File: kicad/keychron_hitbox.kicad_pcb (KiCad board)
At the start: 2 copper layers, 208.5 x 125 mm, 55 parts, among them U1 RP2040-Zero

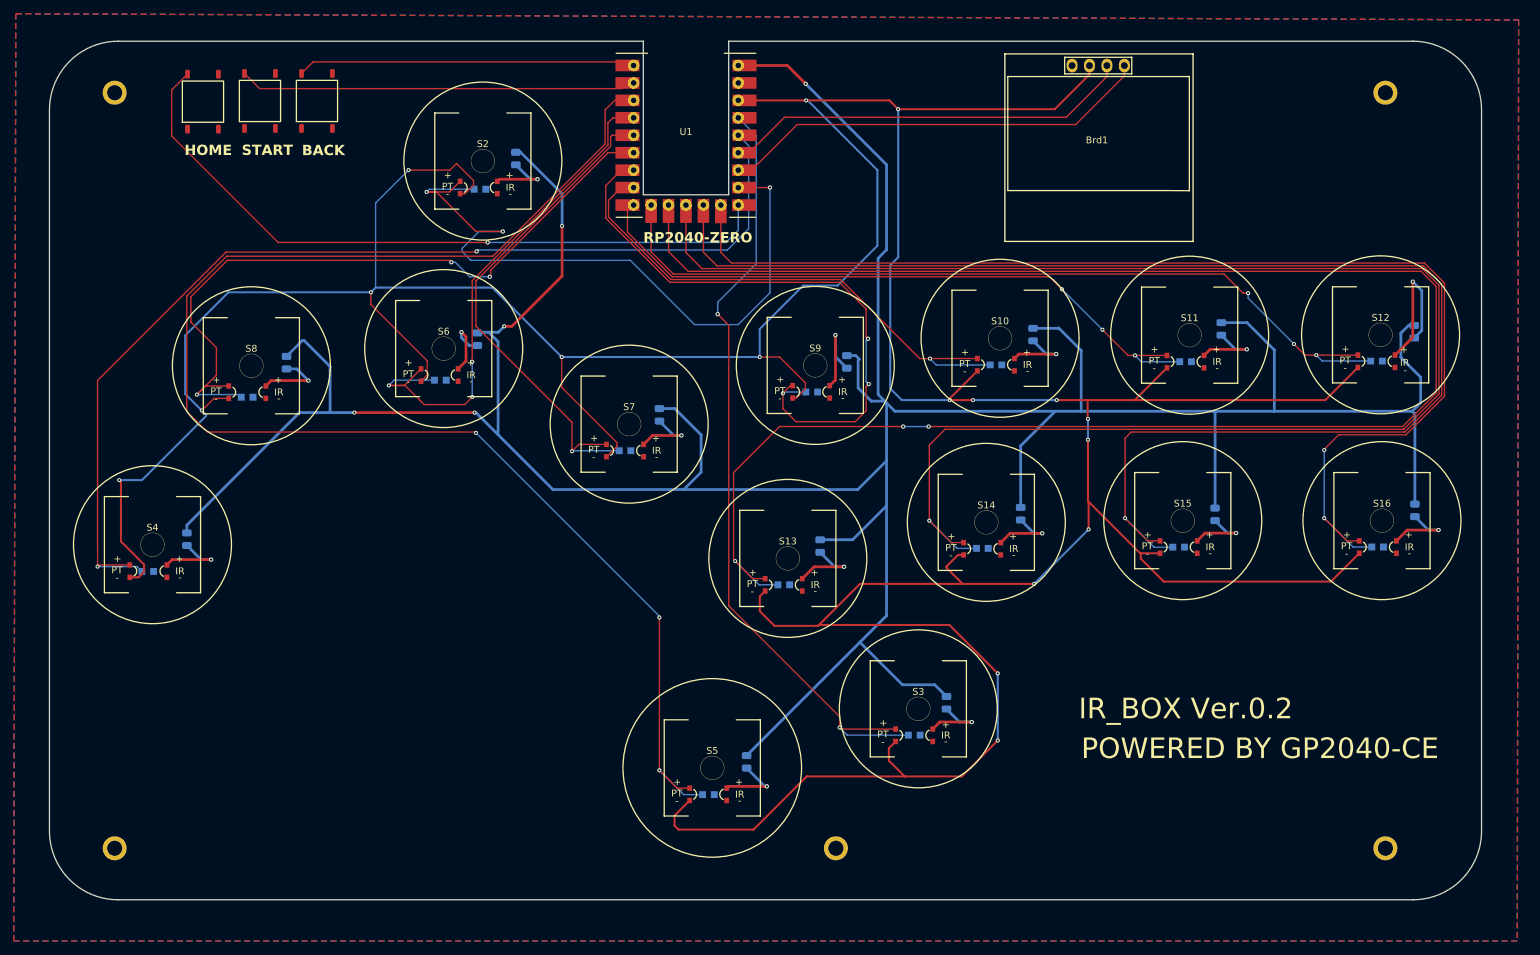
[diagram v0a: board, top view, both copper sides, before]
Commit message: updated seating for OLED & some acrylic designs
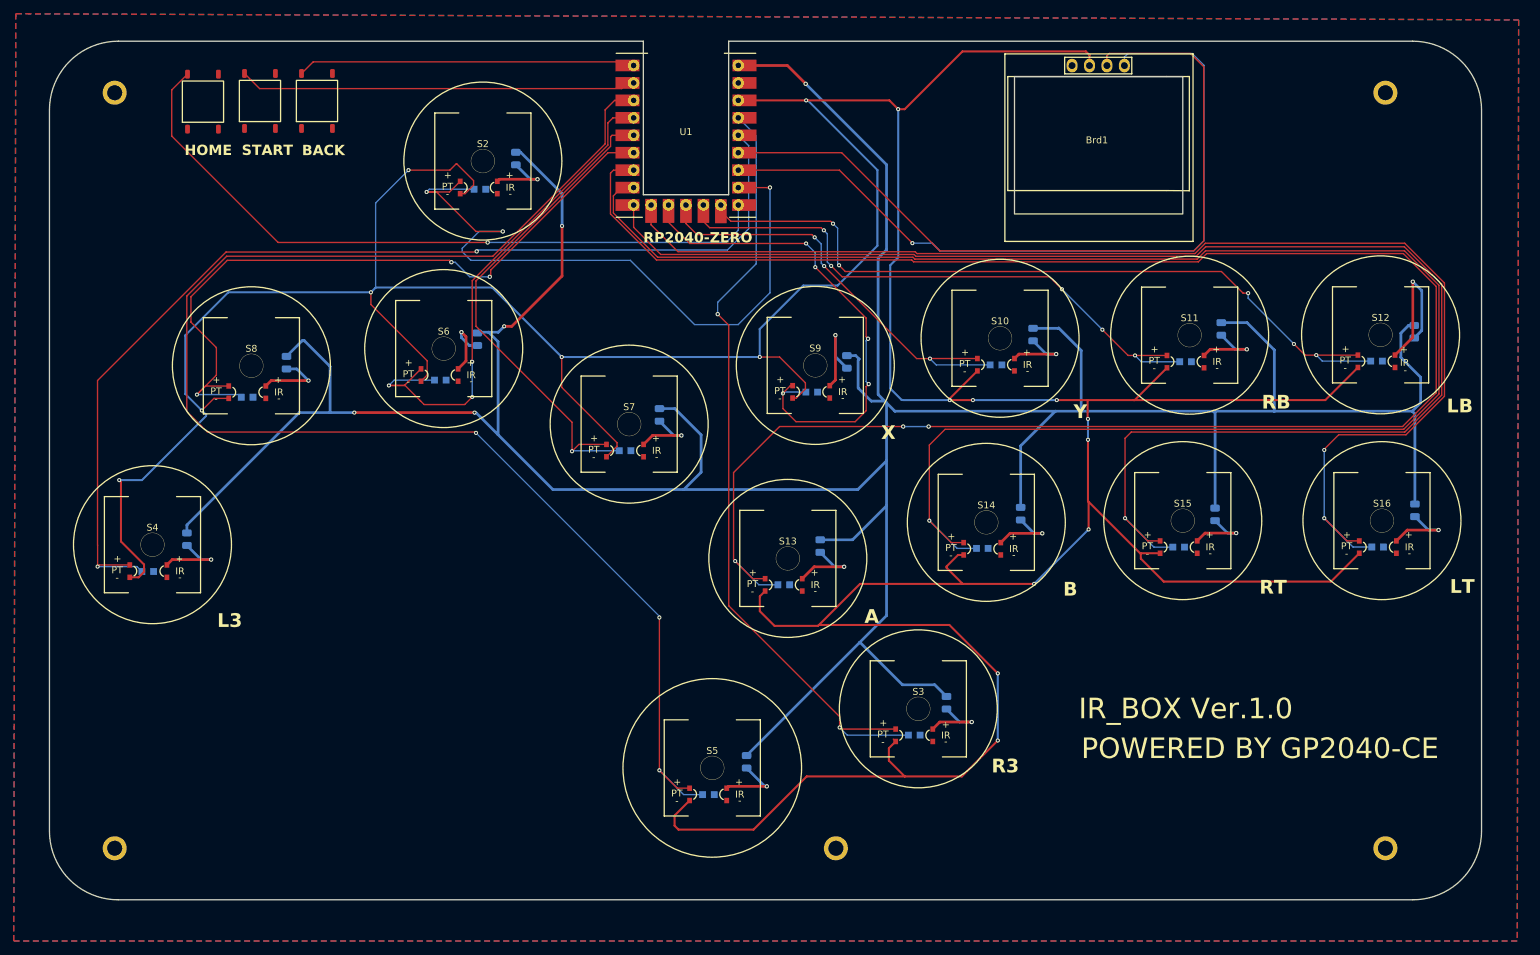
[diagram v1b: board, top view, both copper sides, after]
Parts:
- Brd1: footprint MyFootprints:128x64OLED -> MyFootprints:128x64OLED_hollowed
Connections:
- RP10 pad 2: R2 -> R1
- RP11 pad 2: L2 -> L1
- RP12 pad 2: B3 -> B1
- RP13 pad 2: B4 -> B2
- RP14 pad 2: R1 -> R2
- RP15 pad 2: L1 -> L2
- RP8 pad 2: B1 -> B3
- RP9 pad 2: B2 -> B4
- S10 pad 4: B2 -> B4
- S11 pad 4: R2 -> R1
- S12 pad 4: L2 -> L1
- S13 pad 4: B3 -> B1
- S14 pad 4: B4 -> B2
- S15 pad 4: R1 -> R2
- S16 pad 4: L1 -> L2
- S9 pad 4: B1 -> B3
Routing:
- net B3: track 268.5 -> 73.4 mm, vias 3 -> 5
- net B1: track 88.7 -> 282.8 mm
- net B2: track 77.3 -> 250.5 mm
- net B4: track 236.6 -> 64.1 mm, vias 1 -> 3
- net R2: track 96.8 -> 217.1 mm, vias 3 -> 1
- net R1: track 207.1 -> 87.3 mm, vias 1 -> 5
- net L1: track 176.4 -> 114.1 mm, vias 2 -> 5
- net L2: track 124.7 -> 184.7 mm, vias 3 -> 2
- net SCL: track 59.9 -> 117.7 mm
- net SDA: track 62.5 -> 113.7 mm, vias 0 -> 1
- net 3v3: track 689.3 -> 691.2 mm
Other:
- board text added: "A"
- board text added: "B"
- board text added: "IR_BOX Ver.1.0"
- board text added: "L3"
- board text added: "LB"
- board text added: "LT"
- board text added: "R3"
- board text added: "RB"
- board text added: "RT"
- board text added: "X"
- board text added: "Y"
- board text removed: "IR_BOX Ver.0.2"

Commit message: updated seating for OLED & some acrylic designs
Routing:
- net B2: track 250.5 -> 252.0 mm
- net B1: track 282.8 -> 284.2 mm
- net R3: track 118.3 -> 116.9 mm
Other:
- board text added: "SOCD Priority: Up: HOME + START + Up Neutral: HOME + START + Down Last Wins: HOME + START + LEFT"
- board text added: "While plugging in power: Hold START for web configurator Hold A for Nintendo Switch Hold B for Xinput (Xbox) Hold X for Dinput Hold Y for PS5 Hold RB for Xbox One Hold RT for keyboard"

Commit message: adding version 1.1
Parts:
- added G***: LOGO, MyFootprints:transistor_mask, F.Cu at (71.1, 126.5)
- added R16: R_0805, PCM_Resistor_SMD_AKL:R_0805_2012Metric, B.Cu at (168.4, 41.6)
- added RP16: R_PT, PCM_4ms_Resistor:R_0603, B.Cu at (163.9, 46.2)
- added S1: S2, MyFootprints:Keychron_Optical_Switch_23mm, F.Cu at (164.4, 42.2)
- added U5: RP2040-Zero-extended, MyFootprints:RP2040 Zero zllpin, F.Cu at (125.5, 51.6)
- added U6: ~, MyFootprints:usba_header, F.Cu at (49.6, 54.5)
- U1: value RP2040-Zero -> ~; footprint RP2040-Zero:RP2040 Zero_flipped -> MyFootprints:6x6pushbutton
- moved U1 67.2 mm to (61.0, 34.0), turned to 90 degrees
- moved U3 4.56 mm to (86.5, 34.0)
- moved U2 4.36 mm to (78.0, 34.0)
- moved U4 4.15 mm to (69.5, 34.0)
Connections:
- RP1 pad 2: A2 -> E2
- S2 pad 4: A2 -> E2
- U1 pad 1: 5v -> unconnected-(U1-Pad1)
- U1 pad 2: GND -> A2
- U1 pad 3: 3v3 -> GND
- U1 pad 4: R3 -> unconnected-(U1-Pad4)
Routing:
- net B1: track 284.2 -> 69.8 mm, vias 3 -> 2
- net 3v3: track 691.2 -> 845.2 mm, vias 17 -> 10
- net B2: track 252.0 -> 116.9 mm, vias 1 -> 2
- net UP: track 212.5 -> 111.1 mm, vias 3 -> 1
- net E1: track 0.00 -> 86.5 mm, vias 0 -> 2
- net D-: track 0.00 -> 85.4 mm, vias 0 -> 2
- net D+: track 0.00 -> 83.7 mm, vias 0 -> 2
- net S1: track 48.4 -> 128.1 mm, vias 0 -> 1
- net R2: track 217.1 -> 138.5 mm, vias 1 -> 2
- net S2: track 57.0 -> 129.3 mm, vias 0 -> 1
- net DOWN: track 77.9 -> 121.7 mm, vias 3 -> 1
- net E2: track 0.00 -> 43.7 mm, vias 0 -> 1
- net B3: track 73.4 -> 36.1 mm, vias 5 -> 2
- net L3: track 156.8 -> 121.2 mm, vias 2 -> 3
- net 5v: track 534.2 -> 567.5 mm, vias 5 -> 1
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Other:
- outline, holes or cut-outs redrawn
- board text added: "-"
- board text added: "DOWN"
- board text added: "IR_BOX Ver.1.1"
- board text added: "LEFT"
- board text added: "OPTICAL SWITCH INSIDE"
- board text added: "RIGHT"
- board text added: "UP"
- board text removed: "IR_BOX Ver.1.0"

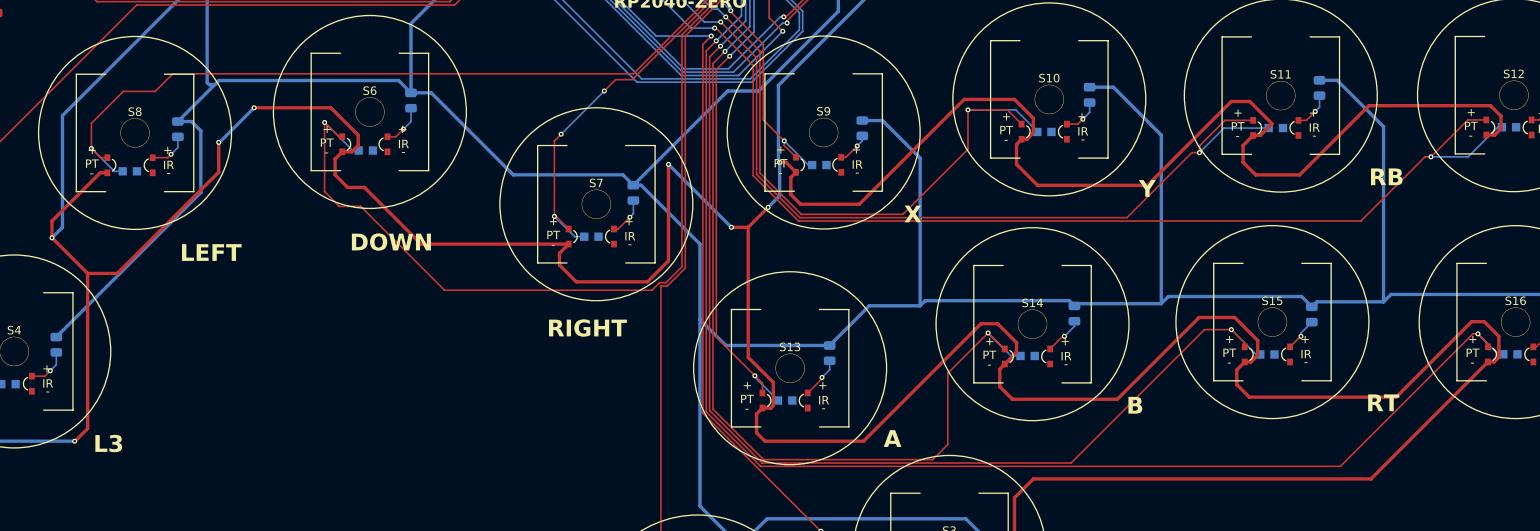
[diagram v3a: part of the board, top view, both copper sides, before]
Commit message: fix 3d file keyswitch plate
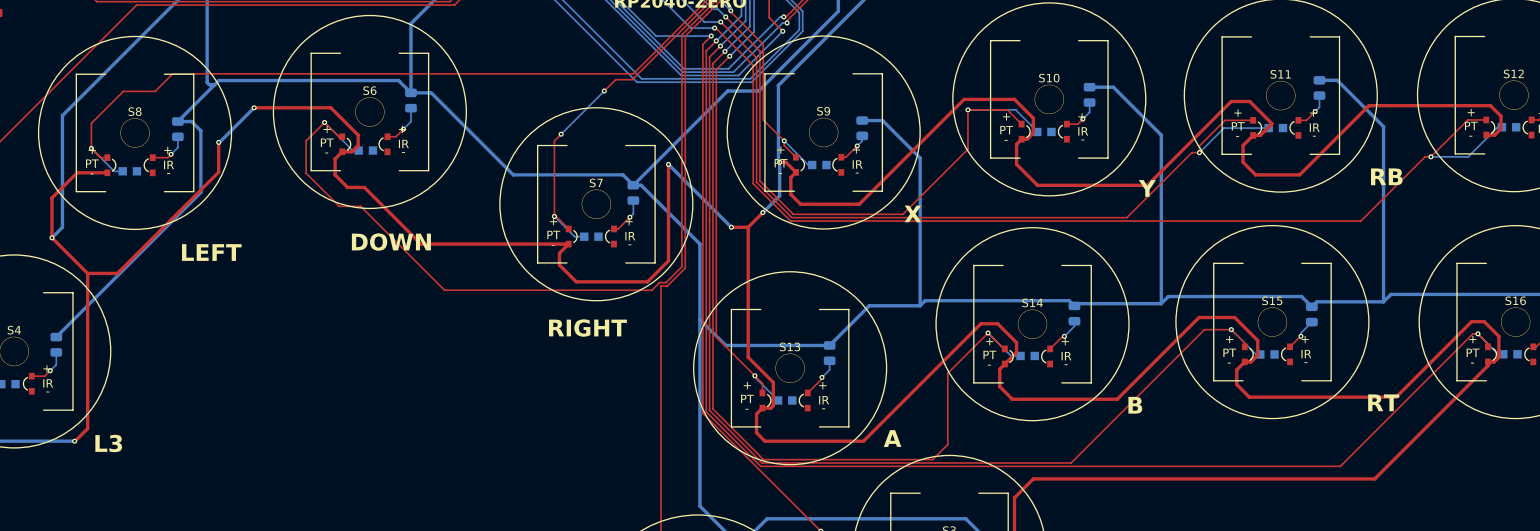
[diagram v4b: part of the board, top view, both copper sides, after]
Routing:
- net 3v3: track 845.2 -> 847.1 mm
- net DOWN: track 121.7 -> 123.5 mm
- net L1: track 141.1 -> 141.7 mm
- net R1: track 111.0 -> 111.6 mm
- net B4: track 84.3 -> 84.9 mm
